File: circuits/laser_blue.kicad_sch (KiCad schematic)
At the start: 10 parts, among them Q4 AO3400A, U8 TLV9001

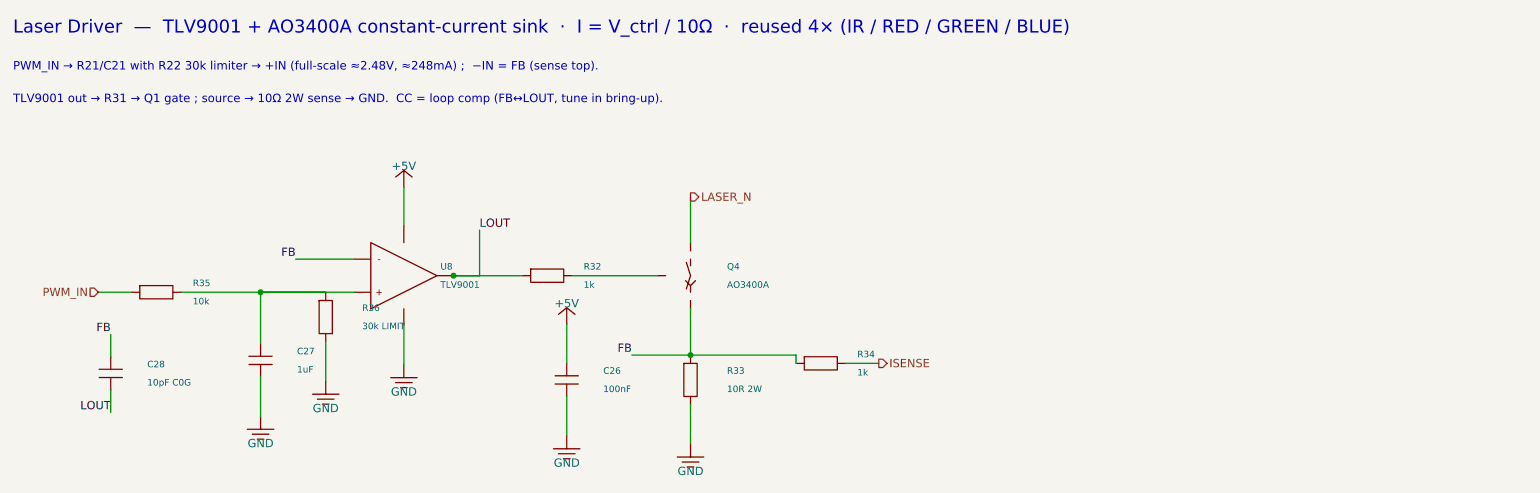
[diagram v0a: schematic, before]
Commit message: chore(circuits): update laser controller release artifacts
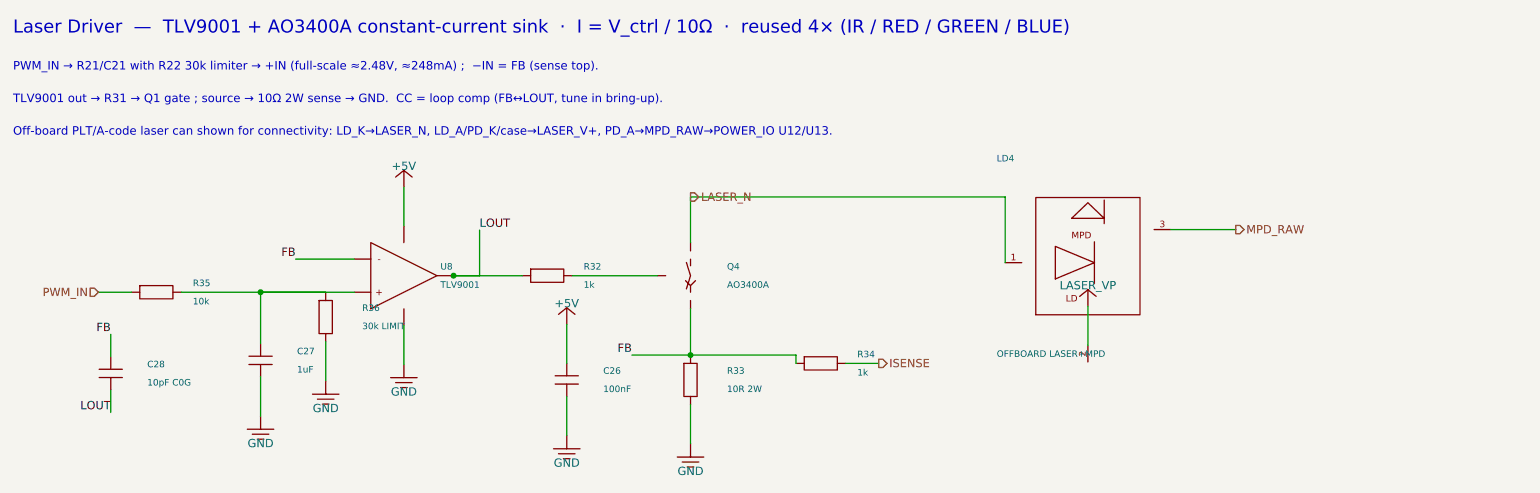
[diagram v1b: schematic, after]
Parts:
- added LD4: OFFBOARD LASER+MPD, symbol viv:LASER_CAN_MON_PD
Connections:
- net LASER_N: now also LD4.1 (LD_K)
- new net LASER_V+: LD4.2 (LD_A/PD_K/CASE)
- new net MPD_RAW: LD4.3 (PD_A)
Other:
- note added: "Off-board PLT/A-code laser can shown for connectivity: LD_K→LASER_N, LD_A/PD_K/case→LASER_V+, PD_A→MPD_RAW→POWER_IO U12/U13."
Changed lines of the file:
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@@
+    )
+  )
+  (symbol (lib_id "viv:LASER_CAN_MON_PD") (at 315 150 0) (unit 1)
+    (in_bom no) (on_board yes) (dnp no)
+    (property "Reference" "LD4" (at 301 134 0) (effects (font (size 1.0 1.0)) (justify left)))
+    (property "Value" "OFFBOARD LASER+MPD" (at 301 164 0) (effects (font (size 1.0 1.0)) (justify left)))
+    (property "Footprint" "" (at 315 150 0) (effects (font (size 1.0 1.0)) hide))
+    (property "Datasheet" "" (at 315 150 0) (effects (font (size 1.0 1.0)) hide))
+    (property "Part Number" "" (at 315 150 0) (effects (font (size 1.0 1.0)) hide))
+    (property "LCSC" "" (at 315 150 0) (effects (font (size 1.0 1.0)) hide))
+    (pin "1")
+    (pin "2")
+    (pin "3")
+    (instances
+      (project "laser_controller"
+        (path "/c1d2e3f4-6000-4000-a000-000000000001" (reference "LD4") (unit 1))
+      )
     )
   )
@@
       (project "laser_controller"
         (path "/c1d2e3f4-6000-4000-a000-000000000001" (reference "#PWR07") (unit 1))
+      )
+    )
+  )
+  (symbol (lib_id "viv:LASER_VP") (at 315 156.7 0) (unit 1)
+    (in_bom no) (on_board yes) (dnp no)
+    (property "Reference" "#PWR08" (at 315 153.7 0) (effects (font (size 1.0 1.0)) hide))
+    (property "Value" "LASER_VP" (at 315 153.5 0) (effects (font (size 1.27 1.27))))
+    (property "Footprint" "" (at 0 0 0) (effects (font (size 1.0 1.0)) hide))
+    (property "Datasheet" "" (at 0 0 0) (effects (font (size 1.0 1.0)) hide))
+    (pin "1")
+    (instances
+      (project "laser_controller"
+        (path "/c1d2e3f4-6000-4000-a000-000000000001" (reference "#PWR08") (unit 1))
       )
     )
@@
   (wire (pts (xy 277.81 165.46) (xy 282.89 165.46)) (stroke (width 0) (type default)))
   (wire (pts (xy 254 146.92) (xy 254 139.92)) (stroke (width 0) (type default)))
+  (wire (pts (xy 254 139.92) (xy 302.3 139.92)) (stroke (width 0) (type default)))
+  (wire (pts (xy 302.3 139.92) (xy 302.3 150)) (stroke (width 0) (type default)))
+  (wire (pts (xy 315 162.7) (xy 315 156.7)) (stroke (width 0) (type default)))
+  (wire (pts (xy 327.7 144.92) (xy 337.7 144.92)) (stroke (width 0) (type default)))
   (wire (pts (xy 202.38 149.46) (xy 193.38 149.46)) (stroke (width 0) (type default)))
   (wire (pts (xy 254 164.19) (xy 245 164.19)) (stroke (width 0) (type default)))
@@
   (hierarchical_label "ISENSE" (shape output) (at 282.89 165.46 0) (effects (font (size 1.27 1.27)) (justify left)))
   (hierarchical_label "LASER_N" (shape output) (at 254 139.92 0) (effects (font (size 1.27 1.27)) (justify left)))
+  (hierarchical_label "MPD_RAW" (shape output) (at 337.7 144.92 0) (effects (font (size 1.27 1.27)) (justify left)))
   (label "FB" (at 193.38 149.46 0) (effects (font (size 1.27 1.27)) (justify right bottom)))
   (label "FB" (at 245 164.19 0) (effects (font (size 1.27 1.27)) (justify right bottom)))
@@
   (text "PWM_IN → R21/C21 with R22 30k limiter → +IN (full-scale ≈2.48V, ≈248mA) ;  −IN = FB (sense top)." (at 150 120 0) (effects (font (size 1.3 1.3)) (justify left)))
   (text "TLV9001 out → R31 → Q1 gate ; source → 10Ω 2W sense → GND.  CC = loop comp (FB↔LOUT, tune in bring-up)." (at 150 125 0) (effects (font (size 1.3 1.3)) (justify left)))
+  (text "Off-board PLT/A-code laser can shown for connectivity: LD_K→LASER_N, LD_A/PD_K/case→LASER_V+, PD_A→MPD_RAW→POWER_IO U12/U13." (at 150 130 0) (effects (font (size 1.3 1.3)) (justify left)))
   (sheet_instances
     (path "/" (page "1"))

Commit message: fix(circuits): import mcu sheet and laser footprints
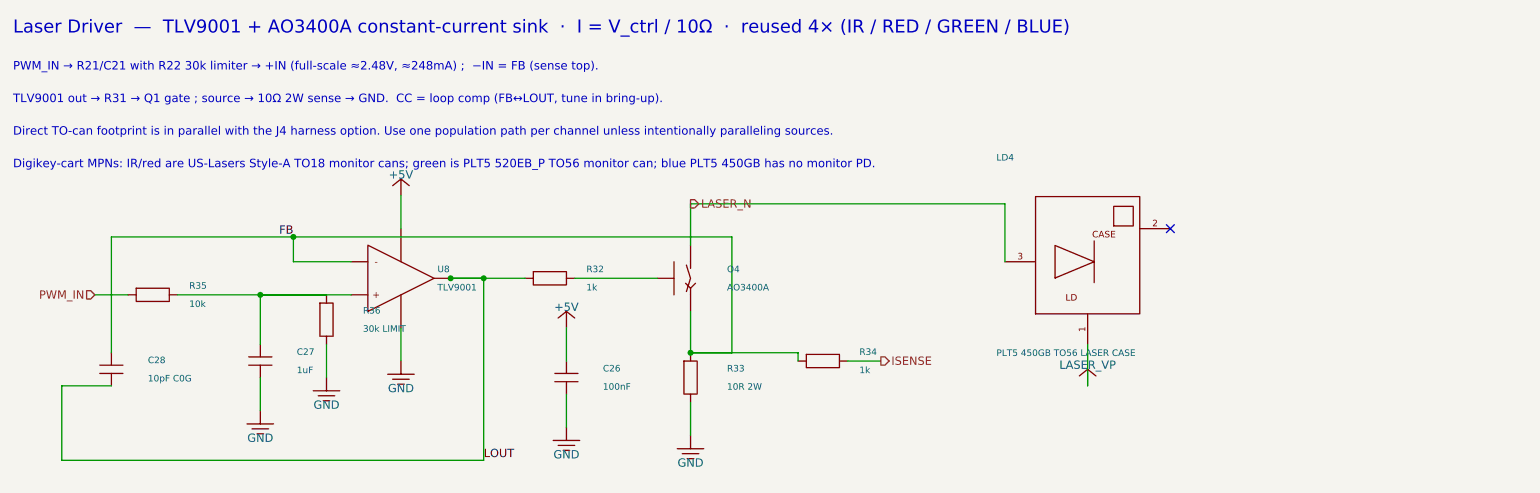
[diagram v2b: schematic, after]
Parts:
- removed C26: 100nF, Capacitor_SMD:C_0402_1005Metric_Pad0.74x0.62mm_HandSolder, symbol viv:C_V
- removed LD4: OFFBOARD LASER+MPD, symbol viv:LASER_CAN_MON_PD
- removed Q4: AO3400A, Package_TO_SOT_SMD:SOT-23, symbol viv:NMOS
- removed R32: 1k, Resistor_SMD:R_0603_1608Metric_Pad0.98x0.95mm_HandSolder, symbol viv:R_H
- removed U8: TLV9001, Package_TO_SOT_SMD:SOT-23-5, symbol viv:TLV9001_SOT23_5
- added C27: 1uF, Capacitor_SMD:C_0402_1005Metric_Pad0.74x0.62mm_HandSolder, symbol viv:C_V
- added C28: 10pF C0G, Capacitor_SMD:C_0603_1608Metric_Pad1.08x0.95mm_HandSolder, symbol viv:C_V
- added R33: 10R 2W, Resistor_SMD:R_2512_6332Metric_Pad1.40x3.35mm_HandSolder, symbol viv:R_V
- added R34: 1k, Resistor_SMD:R_0603_1608Metric_Pad0.98x0.95mm_HandSolder, symbol viv:R_H
- added R35: 10k, Resistor_SMD:R_0603_1608Metric_Pad0.98x0.95mm_HandSolder, symbol viv:R_H
- C26: renamed from R33; value 10R 2W -> 100nF; footprint Resistor_SMD:R_2512_6332Metric_Pad1.40x3.35mm_HandSolder -> Capacitor_SMD:C_0402_1005Metric_Pad0.74x0.62mm_HandSolder; symbol viv:R_V -> viv:C_V; LCSC C5123624 -> C83056; Part Number HoCR2512-2W-10R-1% -> 0402B104K160CT
- LD4: renamed from C27; value 1uF -> PLT5 450GB TO56 LASER CASE; footprint Capacitor_SMD:C_0402_1005Metric_Pad0.74x0.62mm_HandSolder -> OptoDevice:LaserDiode_TO56-3; symbol viv:C_V -> viv:LASER_CAN_DIODE_CASE; LCSC C52923 -> (none); Part Number CL05A105KA5NQNC -> PLT5 450GB; now left out of the parts list
- Q4: renamed from C28; value 10pF C0G -> AO3400A; footprint Capacitor_SMD:C_0603_1608Metric_Pad1.08x0.95mm_HandSolder -> Package_TO_SOT_SMD:SOT-23; symbol viv:C_V -> viv:NMOS; LCSC C106245 -> C20917; Part Number CC0603JRNPO9BN100 -> AO3400A
- R32: renamed from R34; LCSC C21190 -> C2907002; Part Number 0603WAF1001T5E -> FRC0603F1001TS
- U8: renamed from R35; value 10k -> TLV9001; footprint Resistor_SMD:R_0603_1608Metric_Pad0.98x0.95mm_HandSolder -> Package_TO_SOT_SMD:SOT-23-5; symbol viv:R_H -> viv:TLV9001_SOT23_5; LCSC C269701 -> C398363; Part Number 0603WAF1002T5E -> TLV9001IDBVR
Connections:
- net +5V: now also C26.1, U8.5 (V+)
- net FB: now also Q4.2 (S), U8.4 (-), C28.1, R33.1, R34.1; no longer C26.1, Q4.1, R32.1
- net GND: now also U8.2 (V-), C27.2, R33.2; no longer LD4.2
- net ISENSE: now also R34.2; no longer R32.2
- net LASER_N: now also LD4.3 (LD_K), Q4.3 (D)
- net LASER_V+: now also LD4.1 (LD_A)
- net LOUT: now also R32.1, U8.1, C28.2; no longer Q4.2
- net PWM_IN: now also R35.1; no longer U8.1
- new net: C27.1, R35.2, R36.1, U8.3 (+)
- new net: Q4.1 (G), R32.2
- no-connect marks 0 -> 1
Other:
- note added: "Digikey-cart MPNs: IR/red are US-Lasers Style-A TO18 monitor cans; green is PLT5 520EB_P TO56 monitor can; blue PLT5 450GB has no monitor PD."
- note added: "Direct TO-can footprint is in parallel with the J4 harness option. Use one population path per channel unless intentionally paralleling sources."
- note removed: "Off-board PLT/A-code laser can shown for connectivity: LD_K→LASER_N, LD_A/PD_K/case→LASER_V+, PD_A→MPD_RAW→POWER_IO U12/U13."
- moved on the sheet: R32

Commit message: save laser controller schematic and layout state
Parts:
- removed R35: 10k, Resistor_SMD:R_0603_1608Metric_Pad0.98x0.95mm_HandSolder, symbol viv:R_H
- removed R36: 30k LIMIT, Resistor_SMD:R_0603_1608Metric_Pad0.98x0.95mm_HandSolder, symbol viv:R_V
- added Q4: AO3400A, Package_TO_SOT_SMD:SOT-23, symbol viv:NMOS
- added R32: 1k, Resistor_SMD:R_0603_1608Metric_Pad0.98x0.95mm_HandSolder, symbol viv:R_H
- R35: renamed from R32; value 1k -> 10k; LCSC C2907002 -> C844918; Part Number FRC0603F1001TS -> CRCW060310K0FKEA
- R36: renamed from Q4; value AO3400A -> 30k LIMIT; footprint Package_TO_SOT_SMD:SOT-23 -> Resistor_SMD:R_0603_1608Metric_Pad0.98x0.95mm_HandSolder; symbol viv:NMOS -> viv:R_V; LCSC C20917 -> C22984; Part Number AO3400A -> 0603WAF3002T5E
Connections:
- net FB: now also Q4.2 (S); no longer R36.2 (S)
- net GND: now also R36.2
- net LASER_N: now also Q4.3 (D); no longer R36.3 (D)
- net LOUT: now also R32.1; no longer R35.1
- net PWM_IN: now also R35.1
- net at C27.1, U8.3 (+): now also R35.2, R36.1
- new net: Q4.1 (G), R32.2
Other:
- moved on the sheet: R35

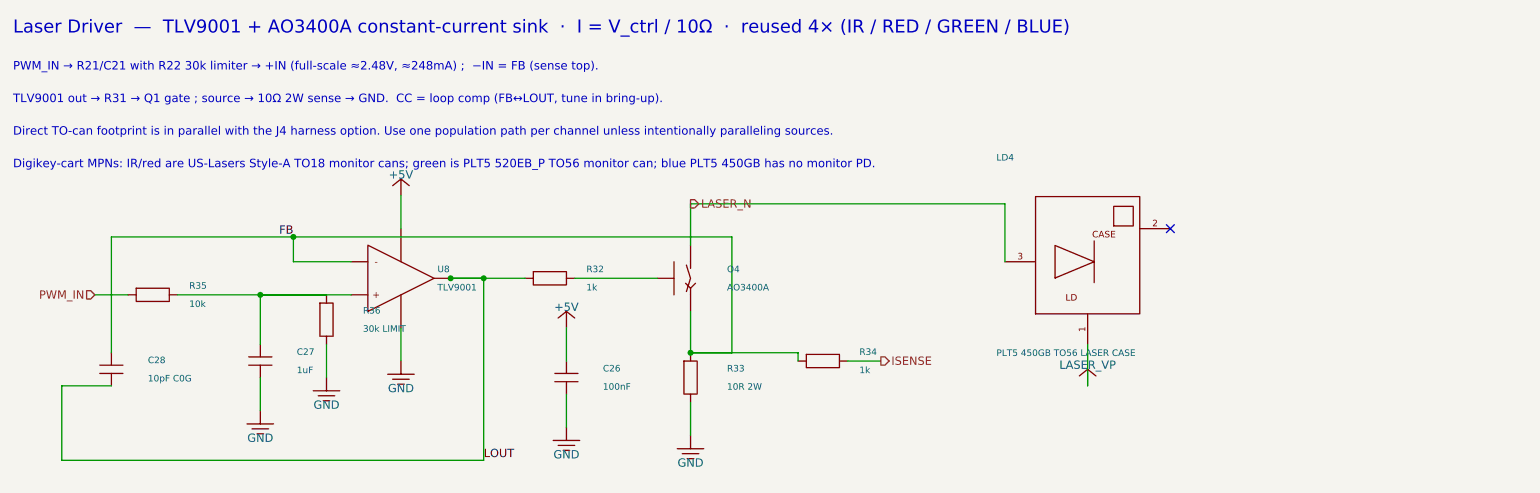
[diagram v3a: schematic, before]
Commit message: save current laser controller recovery state
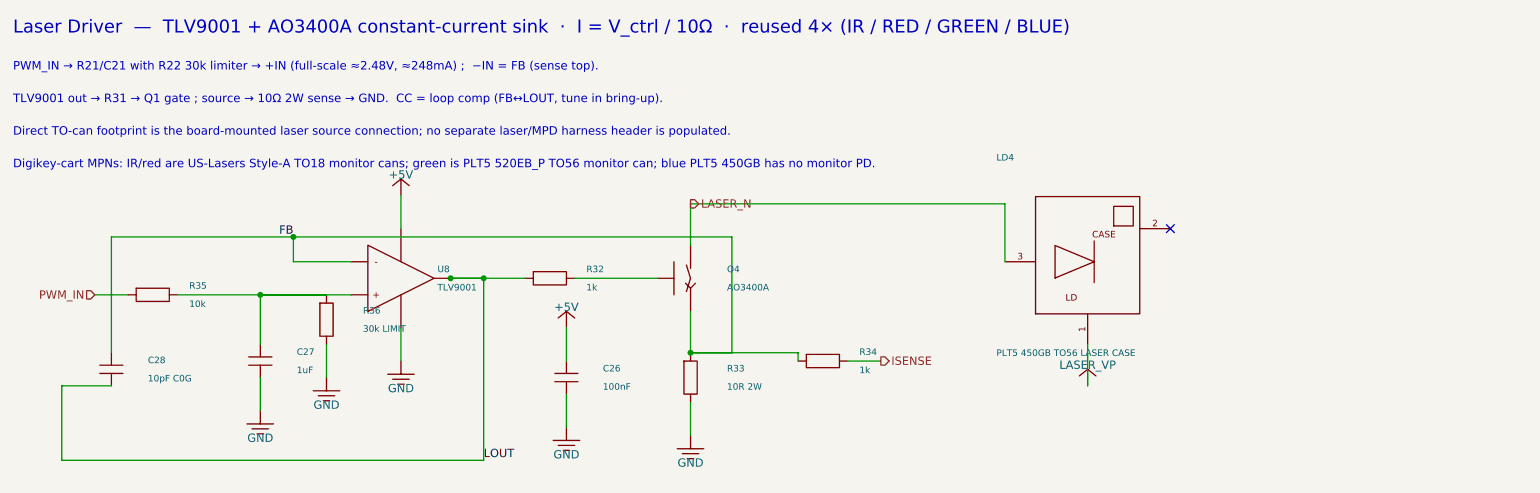
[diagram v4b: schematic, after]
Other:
- note added: "Direct TO-can footprint is the board-mounted laser source connection; no separate laser/MPD harness header is populated."
- note removed: "Direct TO-can footprint is in parallel with the J4 harness option. Use one population path per channel unless intentionally paralleling sources."
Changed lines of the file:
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@@
   (text "PWM_IN → R21/C21 with R22 30k limiter → +IN (full-scale ≈2.48V, ≈248mA) ;  −IN = FB (sense top)." (at 150 120 0) (effects (font (size 1.3 1.3)) (justify left)))
   (text "TLV9001 out → R31 → Q1 gate ; source → 10Ω 2W sense → GND.  CC = loop comp (FB↔LOUT, tune in bring-up)." (at 150 125 0) (effects (font (size 1.3 1.3)) (justify left)))
-  (text "Direct TO-can footprint is in parallel with the J4 harness option. Use one population path per channel unless intentionally paralleling sources." (at 150 130 0) (effects (font (size 1.3 1.3)) (justify left)))
+  (text "Direct TO-can footprint is the board-mounted laser source connection; no separate laser/MPD harness header is populated." (at 150 130 0) (effects (font (size 1.3 1.3)) (justify left)))
   (text "Digikey-cart MPNs: IR/red are US-Lasers Style-A TO18 monitor cans; green is PLT5 520EB_P TO56 monitor can; blue PLT5 450GB has no monitor PD." (at 150 135 0) (effects (font (size 1.3 1.3)) (justify left)))
   (sheet_instances
